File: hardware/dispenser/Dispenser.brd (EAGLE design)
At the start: 73.7 x 75.6 mm, 64 parts, among them J1 AVR_Prog, J2 RJ45-8PTH, Q1 NFET-SO8, Q2 NFET, Q3 NFET, Q4 NFET, Q5 MOSFET-NCHANNELSMD, U1 ATMEGA168, U10 HALL-EFFECT, U2 OPAMP-DUAL, U3 OPTO-TLP185, U4 MPX10DP, U5 VREG-5V-LDO-AP1117SOT89-3L, U6 WS2801, U7 HALL-EFFECT, U8 HALL-EFFECT, U9 HALL-EFFECT

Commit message: Dispener updates
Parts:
- PL1: value M -> Motor Connector
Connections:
- net CURRENT_SENSE renamed 1/4W
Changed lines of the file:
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@@
 <element name="Q3" library="SparkFun-DiscreteSemi" package="SOT23-3" value="NFET" x="46.863" y="64.262" rot="R270"/>
 <element name="Q4" library="SparkFun-DiscreteSemi" package="SOT23-3" value="NFET" x="42.7482" y="64.262" rot="R270"/>
-<element name="PL1" library="con-hirose-df3" package="DF3P-02" value="M" x="36.83" y="9.144" locked="yes"/>
+<element name="PL1" library="con-hirose-df3" package="DF3P-02" value="Motor Connector" x="36.83" y="9.144" locked="yes"/>
 <element name="U5" library="pierre" package="SOT89-3L" value="VREG-5V-LDO-AP1117SOT89-3L" x="25.019" y="12.7"/>
 <element name="C9" library="SparkFun-Passives" package="0603-CAP" value="10u" x="29.464" y="12.192" rot="R90"/>
@@
 <contactref element="Q5" pad="2"/>
 <contactref element="R7" pad="1"/>
-<wire x1="68.8086" y1="41.1924" x2="68.961" y2="46.951" width="0" layer="19" extent="1-1"/>
-<wire x1="60.2234" y1="40.3924" x2="63.881" y2="38.227" width="0" layer="19" extent="1-1"/>
-<wire x1="55.626" y1="44.577" x2="55.2568" y2="42.3028" width="0" layer="19" extent="1-1"/>
-<wire x1="51.663334375" y1="44.867246875" x2="55.626" y2="44.577" width="0" layer="19" extent="16-16"/>
-<wire x1="62.777" y1="33.655" x2="63.881" y2="38.227" width="0" layer="19" extent="1-1"/>
-<wire x1="66.548" y1="29.718" x2="62.777" y2="33.655" width="0" layer="19" extent="1-1"/>
-<wire x1="42.96225" y1="53.56833125" x2="51.663334375" y2="44.867246875" width="0" layer="19" extent="16-16"/>
-<wire x1="34.925" y1="60.325" x2="42.96225" y2="53.56833125" width="0" layer="19" extent="1-16"/>
-<wire x1="26.8868" y1="64.6684" x2="32.302" y2="65.024" width="0" layer="19" extent="1-1"/>
-<wire x1="30.697753125" y1="53.56833125" x2="32.302" y2="59.944" width="0" layer="19" extent="1-16"/>
-<wire x1="21.99666875" y1="44.867246875" x2="30.697753125" y2="53.56833125" width="0" layer="19" extent="16-16"/>
-<wire x1="11.684" y1="41.402" x2="21.99666875" y2="44.867246875" width="0" layer="19" extent="16-16"/>
-<wire x1="11.938" y1="34.456" x2="11.6048" y2="39.0144" width="0" layer="19" extent="1-1"/>
-<wire x1="15.6718" y1="25.8318" x2="11.899" y2="34.417" width="0" layer="19" extent="1-1"/>
-<wire x1="11.088" y1="22.86" x2="15.6718" y2="22.0082" width="0" layer="19" extent="1-1"/>
-<wire x1="11.088" y1="19.685" x2="11.088" y2="22.86" width="0" layer="19" extent="1-1"/>
-<wire x1="19.05" y1="16.51" x2="15.748" y2="21.932" width="0" layer="19" extent="1-1"/>
-<wire x1="29.464" y1="13.042" x2="23.519" y2="11.45" width="0" layer="19" extent="1-1"/>
+<wire x1="55.88" y1="13.335" x2="53.379" y2="14.732" width="0" layer="19" extent="1-1"/>
 <wire x1="-3.595" y1="25.908" x2="8.255" y2="22.86" width="0" layer="19" extent="1-1"/>
 <wire x1="-6.543" y1="21.86" x2="-3.595" y2="25.908" width="0" layer="19" extent="1-1"/>
 <wire x1="-5.345" y1="32.258" x2="-3.595" y2="25.908" width="0" layer="19" extent="1-1"/>
-<wire x1="44.348" y1="17.399" x2="29.464" y2="14.859" width="0" layer="19" extent="1-1"/>
-<wire x1="53.379" y1="14.732" x2="44.348" y2="17.399" width="0" layer="19" extent="1-1"/>
-<wire x1="55.88" y1="13.335" x2="53.379" y2="14.732" width="0" layer="19" extent="1-1"/>
-<wire x1="49.6824" y1="3.5188" x2="55.88" y2="11.811" width="0" layer="19" extent="16-16"/>
-<wire x1="42.164" y1="3.595" x2="49.6824" y2="3.5188" width="0" layer="19" extent="16-16"/>
 </signal>
 <signal name="5V">
@@
 <wire x1="33.528" y1="12.4968" x2="33.4518" y2="12.573" width="0.4064" layer="1"/>
 <contactref element="D1" pad="A"/>
-<wire x1="30.988" y1="12.573" x2="34.045" y2="-1.778" width="0" layer="19" extent="1-1"/>
-</signal>
-<signal name="CURRENT_SENSE">
+<wire x1="34.045" y1="-1.778" x2="34.306" y2="10.144" width="0" layer="19" extent="1-1"/>
+</signal>
+<signal name="1/4W">
 <contactref element="Q1" pad="1"/>
 <contactref element="Q1" pad="2"/>
@@
 <wire x1="20.7264" y1="44.6024" x2="20.701" y2="44.577" width="0.4064" layer="16"/>
 <contactref element="R1" pad="2"/>
-<wire x1="47.586" y1="67.564" x2="51.904" y2="67.564" width="0" layer="19" extent="1-1"/>
-<wire x1="43.5982" y1="67.564" x2="47.586" y2="67.564" width="0" layer="19" extent="1-1"/>
-<wire x1="37.802" y1="67.564" x2="43.5982" y2="67.564" width="0" layer="19" extent="1-1"/>
-<wire x1="38.1" y1="58.84" x2="37.802" y2="67.564" width="0" layer="19" extent="1-16"/>
-<wire x1="26.836" y1="67.056" x2="30.9" y2="58.84" width="0" layer="19" extent="1-16"/>
-<wire x1="52.2732" y1="46.1518" x2="45.974" y2="53.213" width="0" layer="19" extent="16-16"/>
-<wire x1="57.7088" y1="43.981" x2="52.959" y2="43.434" width="0" layer="19" extent="1-16"/>
-<wire x1="60.2234" y1="42.7924" x2="57.7088" y2="43.981" width="0" layer="19" extent="1-1"/>
-<wire x1="68.8086" y1="41.9924" x2="60.2234" y2="42.7924" width="0" layer="19" extent="1-1"/>
-<wire x1="68.8086" y1="40.3924" x2="68.8086" y2="41.9924" width="0" layer="19" extent="1-1"/>
-<wire x1="68.961" y1="45.251" x2="68.8086" y2="41.9924" width="0" layer="19" extent="1-1"/>
-<wire x1="63.031" y1="31.496" x2="68.8086" y2="40.3924" width="0" layer="19" extent="1-1"/>
-<wire x1="62.738" y1="26.67" x2="63.031" y2="31.496" width="0" layer="19" extent="1-1"/>
-<wire x1="53.975" y1="27.559" x2="62.738" y2="26.67" width="0" layer="19" extent="1-1"/>
-<wire x1="11.938" y1="36.156" x2="19.90916875" y2="44.577" width="0" layer="19" extent="1-16"/>
-<wire x1="11.8618" y1="31.0642" x2="11.938" y2="36.156" width="0" layer="19" extent="1-1"/>
-<wire x1="12.788" y1="19.685" x2="11.8618" y2="31.0642" width="0" layer="19" extent="1-1"/>
-<wire x1="24.726" y1="17.399" x2="12.788" y2="19.685" width="0" layer="19" extent="1-1"/>
-<wire x1="25.019" y1="14.05" x2="24.726" y2="17.399" width="0" layer="19" extent="1-1"/>
-<wire x1="25.019" y1="11.75" x2="25.019" y2="14.05" width="0" layer="19" extent="1-1"/>
-<wire x1="41.529" y1="9.056" x2="25.019" y2="11.75" width="0" layer="19" extent="1-1"/>
-<wire x1="-6.643" y1="19.812" x2="12.788" y2="19.685" width="0" layer="19" extent="1-1"/>
+<wire x1="12.788" y1="19.685" x2="-6.643" y2="19.812" width="0" layer="19" extent="1-1"/>
 </signal>
 <signal name="LED_CLK">
@@
 <contactref element="D1" pad="C"/>
 <wire x1="38.83" y1="4.015" x2="38.345" y2="-1.778" width="0" layer="19" extent="1-16"/>
-<wire x1="38.83" y1="5.715" x2="38.83" y2="4.015" width="0" layer="19" extent="16-16"/>
-<wire x1="38.83" y1="7.415" x2="38.83" y2="5.715" width="0" layer="19" extent="16-16"/>
-<wire x1="37.83" y1="10.144" x2="38.83" y2="7.415" width="0" layer="19" extent="16-16"/>
-<wire x1="42.164" y1="5.295" x2="38.83" y2="5.715" width="0" layer="19" extent="16-16"/>
-<wire x1="46.99" y1="9.271" x2="42.164" y2="5.295" width="0" layer="19" extent="16-16"/>
-<wire x1="49.6824" y1="5.2188" x2="46.99" y2="9.271" width="0" layer="19" extent="16-16"/>
 </signal>
 <signal name="N$38">

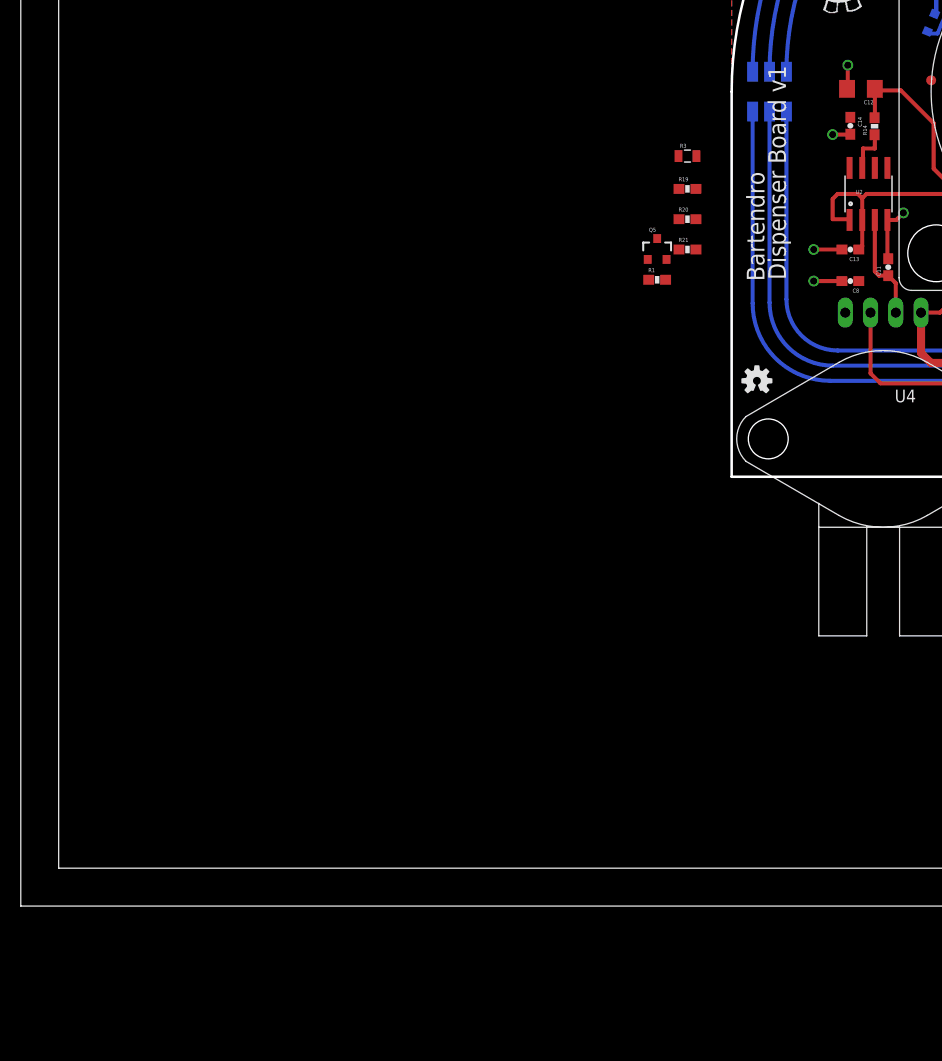
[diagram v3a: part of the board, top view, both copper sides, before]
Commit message: Current sense cap to 100u, and opto inputs changed again
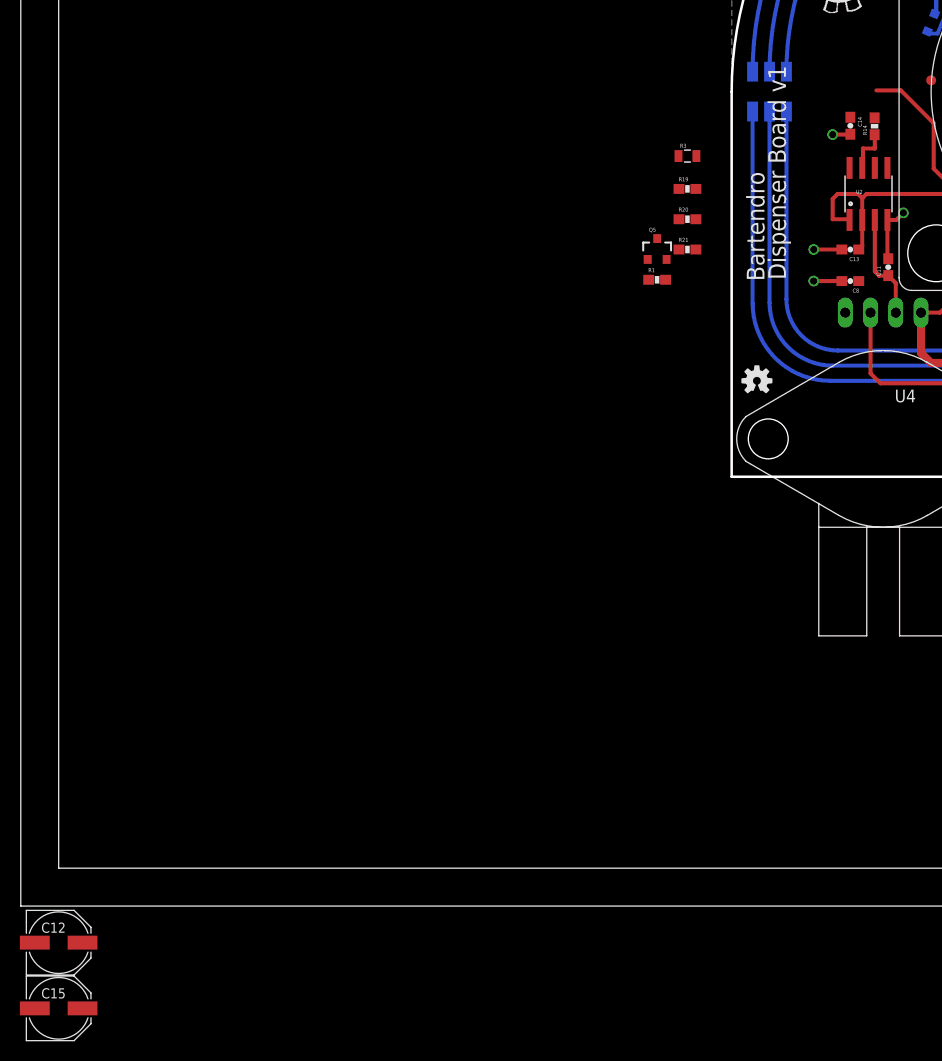
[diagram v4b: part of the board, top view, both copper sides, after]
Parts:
- added C15: 47u 35V, SparkFun-Capacitors:PANASONIC_D
- C12: value 10u -> 100u 6.3V; device SparkFun-Capacitors:1206 -> SparkFun-Capacitors:PANASONIC_D
- moved C12 117.8 mm to (-67.7, -46.9), turned to 0 degrees
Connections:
- new net N$16: R7.2, U3.1
- net 3.3V: now also R7.1
- net CUR_SEN: now also C12.+; no longer C12.1
- net GND: now also C12.-; no longer C12.2, R7.1
- net MOT_CTL: now also U3.3; no longer U3.1
- net N$15: now also C15.-; no longer R7.2, U3.3
- net VIN: now also C15.+
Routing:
- net CUR_SEN: track 62.8 -> 59.7 mm
- net GND: track 94.6 -> 92.2 mm, vias 15 -> 14
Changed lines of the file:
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@@
 <element name="R11" library="SparkFun-Resistors" package="0603-RES" value="33" x="27.7368" y="64.6684" rot="R180"/>
 <element name="R2" library="SparkFun-Resistors" package="0603-RES" value="10k" x="54.1528" y="17.4244" rot="R180"/>
-<element name="C12" library="SparkFun-Capacitors" package="1206" value="10u" x="13.0048" y="39.0144" rot="R180"/>
 <element name="R14" library="SparkFun-Resistors" package="0603-RES" value="1k" x="14.3764" y="35.2552" rot="R90"/>
 <element name="C13" library="SparkFun" package="0603-CAP" value="100n" x="11.938" y="22.86" rot="R180"/>
@@
 <attribute name="PROD_ID" value="DIO-09886" x="36.195" y="-1.778" size="1.778" layer="27" display="off"/>
 </element>
+<element name="C12" library="SparkFun-Capacitors" package="PANASONIC_D" value="100u 6.3V" x="-67.691" y="-46.863"/>
+<element name="C15" library="SparkFun-Capacitors" package="PANASONIC_D" value="47u 35V" x="-67.691" y="-53.467"/>
 </elements>
 <signals>
@@
 <contactref element="R11" pad="2"/>
 <contactref element="R2" pad="1"/>
-<contactref element="C12" pad="2"/>
 <contactref element="C13" pad="2"/>
 <contactref element="C14" pad="2"/>
@@
 <wire x1="68.8086" y1="41.1924" x2="66.8464" y2="41.1924" width="0.4064" layer="1"/>
 <wire x1="68.853" y1="41.148" x2="68.8086" y2="41.1924" width="0.254" layer="1"/>
-<wire x1="11.6048" y1="39.0144" x2="11.684" y2="39.0936" width="0.4064" layer="1"/>
-<wire x1="11.684" y1="39.0936" x2="11.684" y2="41.402" width="0.4064" layer="1"/>
-<via x="11.684" y="41.402" extent="1-16" drill="0.7"/>
 <wire x1="15.6718" y1="25.8318" x2="16.5608" y2="25.8318" width="0.4064" layer="1"/>
 <wire x1="16.5608" y1="25.8318" x2="17.272" y2="26.543" width="0.4064" layer="1"/>
@@
 <contactref element="R20" pad="2"/>
 <contactref element="Q5" pad="2"/>
-<contactref element="R7" pad="1"/>
-<wire x1="55.88" y1="13.335" x2="53.379" y2="14.732" width="0" layer="19" extent="1-1"/>
-<wire x1="-3.595" y1="25.908" x2="8.255" y2="22.86" width="0" layer="19" extent="1-1"/>
-<wire x1="-6.543" y1="21.86" x2="-3.595" y2="25.908" width="0" layer="19" extent="1-1"/>
+<contactref element="C12" pad="-"/>
+<wire x1="-6.543" y1="21.86" x2="-70.091" y2="-46.863" width="0" layer="19" extent="1-1"/>
+<wire x1="-3.595" y1="25.908" x2="-6.543" y2="21.86" width="0" layer="19" extent="1-1"/>
 <wire x1="-5.345" y1="32.258" x2="-3.595" y2="25.908" width="0" layer="19" extent="1-1"/>
+<wire x1="8.255" y1="22.86" x2="-3.595" y2="25.908" width="0" layer="19" extent="1-1"/>
+<wire x1="11.088" y1="19.685" x2="11.088" y2="22.86" width="0" layer="19" extent="1-1"/>
+<wire x1="15.6718" y1="22.0082" x2="11.088" y2="22.86" width="0" layer="19" extent="1-1"/>
+<wire x1="19.05" y1="16.51" x2="15.748" y2="21.932" width="0" layer="19" extent="1-1"/>
+<wire x1="29.464" y1="13.042" x2="23.519" y2="11.45" width="0" layer="19" extent="1-1"/>
+<wire x1="11.899" y1="34.417" x2="15.6718" y2="25.8318" width="0" layer="19" extent="1-1"/>
+<wire x1="21.99666875" y1="44.867246875" x2="11.938" y2="34.456" width="0" layer="19" extent="1-16"/>
+<wire x1="30.697753125" y1="53.56833125" x2="21.99666875" y2="44.867246875" width="0" layer="19" extent="16-16"/>
+<wire x1="32.302" y1="59.944" x2="30.697753125" y2="53.56833125" width="0" layer="19" extent="1-16"/>
+<wire x1="26.8868" y1="64.6684" x2="32.302" y2="65.024" width="0" layer="19" extent="1-1"/>
+<wire x1="42.96225" y1="53.56833125" x2="34.925" y2="60.325" width="0" layer="19" extent="1-16"/>
+<wire x1="51.663334375" y1="44.867246875" x2="42.96225" y2="53.56833125" width="0" layer="19" extent="16-16"/>
+<wire x1="55.626" y1="44.577" x2="51.663334375" y2="44.867246875" width="0" layer="19" extent="16-16"/>
+<wire x1="55.2568" y1="42.3028" x2="55.626" y2="44.577" width="0" layer="19" extent="1-1"/>
+<wire x1="63.881" y1="38.227" x2="60.2234" y2="40.3924" width="0" layer="19" extent="1-1"/>
+<wire x1="62.777" y1="33.655" x2="63.881" y2="38.227" width="0" layer="19" extent="1-1"/>
+<wire x1="66.548" y1="29.718" x2="62.777" y2="33.655" width="0" layer="19" extent="1-1"/>
+<wire x1="68.961" y1="46.951" x2="68.8086" y2="41.1924" width="0" layer="19" extent="1-1"/>
+<wire x1="44.348" y1="17.399" x2="29.464" y2="14.859" width="0" layer="19" extent="1-1"/>
+<wire x1="55.0028" y1="17.4244" x2="44.348" y2="17.399" width="0" layer="19" extent="1-1"/>
+<wire x1="49.6824" y1="3.5188" x2="55.88" y2="11.811" width="0" layer="19" extent="16-16"/>
+<wire x1="42.164" y1="3.595" x2="49.6824" y2="3.5188" width="0" layer="19" extent="16-16"/>
 </signal>
 <signal name="5V">
@@
 <wire x1="20.7264" y1="44.6024" x2="20.701" y2="44.577" width="0.4064" layer="16"/>
 <contactref element="R1" pad="2"/>
-<wire x1="12.788" y1="19.685" x2="-6.643" y2="19.812" width="0" layer="19" extent="1-1"/>
+<contactref element="R7" pad="1"/>
+<wire x1="47.586" y1="67.564" x2="51.904" y2="67.564" width="0" layer="19" extent="1-1"/>
+<wire x1="43.5982" y1="67.564" x2="47.586" y2="67.564" width="0" layer="19" extent="1-1"/>
+<wire x1="37.802" y1="67.564" x2="43.5982" y2="67.564" width="0" layer="19" extent="1-1"/>
+<wire x1="38.1" y1="58.84" x2="37.802" y2="67.564" width="0" layer="19" extent="1-16"/>
+<wire x1="26.836" y1="67.056" x2="30.9" y2="58.84" width="0" layer="19" extent="1-16"/>
+<wire x1="52.2732" y1="46.1518" x2="45.974" y2="53.213" width="0" layer="19" extent="16-16"/>
+<wire x1="57.7088" y1="43.981" x2="52.959" y2="43.434" width="0" layer="19" extent="1-16"/>
+<wire x1="60.2234" y1="42.7924" x2="57.7088" y2="43.981" width="0" layer="19" extent="1-1"/>
+<wire x1="68.8086" y1="41.9924" x2="60.2234" y2="42.7924" width="0" layer="19" extent="1-1"/>
+<wire x1="68.8086" y1="40.3924" x2="68.8086" y2="41.9924" width="0" layer="19" extent="1-1"/>
+<wire x1="68.961" y1="45.251" x2="68.8086" y2="41.9924" width="0" layer="19" extent="1-1"/>
+<wire x1="63.031" y1="31.496" x2="68.8086" y2="40.3924" width="0" layer="19" extent="1-1"/>
+<wire x1="62.738" y1="26.67" x2="63.031" y2="31.496" width="0" layer="19" extent="1-1"/>
+<wire x1="53.975" y1="27.559" x2="62.738" y2="26.67" width="0" layer="19" extent="1-1"/>
+<wire x1="11.938" y1="36.156" x2="19.90916875" y2="44.577" width="0" layer="19" extent="1-16"/>
+<wire x1="11.8618" y1="31.0642" x2="11.938" y2="36.156" width="0" layer="19" extent="1-1"/>
+<wire x1="12.788" y1="19.685" x2="11.8618" y2="31.0642" width="0" layer="19" extent="1-1"/>
+<wire x1="24.726" y1="17.399" x2="12.788" y2="19.685" width="0" layer="19" extent="1-1"/>
+<wire x1="25.019" y1="14.05" x2="24.726" y2="17.399" width="0" layer="19" extent="1-1"/>
+<wire x1="25.019" y1="11.75" x2="25.019" y2="14.05" width="0" layer="19" extent="1-1"/>
+<wire x1="53.379" y1="14.732" x2="53.975" y2="27.559" width="0" layer="19" extent="1-1"/>
+<wire x1="41.529" y1="9.056" x2="53.379" y2="14.732" width="0" layer="19" extent="1-1"/>
+<wire x1="-6.643" y1="19.812" x2="12.788" y2="19.685" width="0" layer="19" extent="1-1"/>
 </signal>
 <signal name="LED_CLK">
@@
 <signal name="CUR_SEN">
 <contactref element="U1" pad="23"/>
-<contactref element="C12" pad="1"/>
 <contactref element="R14" pad="2"/>
 <wire x1="14.3764" y1="36.1052" x2="14.4048" y2="36.1336" width="0.4064" layer="1"/>
-<wire x1="14.4048" y1="36.1336" x2="14.4048" y2="39.0144" width="0.4064" layer="1"/>
-<wire x1="14.4048" y1="39.0144" x2="14.5572" y2="38.862" width="0.4064" layer="1"/>
 <wire x1="14.5572" y1="38.862" x2="17.018" y2="38.862" width="0.4064" layer="1"/>
 <wire x1="17.018" y1="38.862" x2="20.32" y2="35.56" width="0.4064" layer="1"/>
@@
 <wire x1="44.704" y1="25.146" x2="58.3504" y2="38.7924" width="0.4064" layer="1"/>
 <wire x1="58.3504" y1="38.7924" x2="60.2234" y2="38.7924" width="0.4064" layer="1"/>
+<contactref element="C12" pad="+"/>
+<wire x1="14.3764" y1="36.1052" x2="-65.291" y2="-46.863" width="0" layer="19" extent="1-1"/>
+<wire x1="14.5572" y1="38.862" x2="14.4048" y2="36.1336" width="0" layer="19" extent="1-1"/>
 </signal>
 <signal name="N$17">
@@
 <wire x1="48.006" y1="18.288" x2="48.006" y2="24.257" width="0.254" layer="1"/>
 <wire x1="48.006" y1="24.257" x2="67.316" y2="43.6432" width="0.254" layer="1"/>
-<contactref element="U3" pad="1"/>
-<wire x1="50.648" y1="14.859" x2="48.8696" y2="17.4244" width="0" layer="19" extent="1-1"/>
+<contactref element="U3" pad="3"/>
+<wire x1="50.648" y1="17.399" x2="48.8696" y2="17.4244" width="0" layer="19" extent="1-1"/>
 </signal>
 <signal name="N$6">
@@
 </polygon>
 <contactref element="D1" pad="C"/>
+<contactref element="C15" pad="+"/>
+<wire x1="38.345" y1="-1.778" x2="-65.291" y2="-53.467" width="0" layer="19" extent="1-1"/>
 <wire x1="38.83" y1="4.015" x2="38.345" y2="-1.778" width="0" layer="19" extent="1-16"/>
+<wire x1="38.83" y1="5.715" x2="38.83" y2="4.015" width="0" layer="19" extent="16-16"/>
+<wire x1="38.83" y1="7.415" x2="38.83" y2="5.715" width="0" layer="19" extent="16-16"/>
+<wire x1="37.83" y1="10.144" x2="38.83" y2="7.415" width="0" layer="19" extent="16-16"/>
+<wire x1="42.164" y1="5.295" x2="38.83" y2="5.715" width="0" layer="19" extent="16-16"/>
+<wire x1="46.99" y1="9.271" x2="42.164" y2="5.295" width="0" layer="19" extent="16-16"/>
+<wire x1="49.6824" y1="5.2188" x2="46.99" y2="9.271" width="0" layer="19" extent="16-16"/>
 </signal>
 <signal name="N$38">
@@
 <wire x1="-5.295" y1="28.956" x2="15.6718" y2="31.0642" width="0" layer="19" extent="1-1"/>
 </signal>
+<signal name="N$16">
+<contactref element="R7" pad="2"/>
+<contactref element="U3" pad="1"/>
+<wire x1="50.648" y1="14.859" x2="55.079" y2="14.732" width="0" layer="19" extent="1-1"/>
+</signal>
 <signal name="N$15">
-<contactref element="R7" pad="2"/>
-<contactref element="U3" pad="3"/>
-<wire x1="50.648" y1="17.399" x2="55.079" y2="14.732" width="0" layer="19" extent="1-1"/>
+<contactref element="C15" pad="-"/>
 </signal>
 </signals>
